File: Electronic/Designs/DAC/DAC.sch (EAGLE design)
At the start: 36 parts

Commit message: added new part to dac board
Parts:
- C5, C7: value 0.1uf -> 1uf
- JP1: value (none) -> PWR
- JP3: value (none) -> DIGITAL
- U$4: value OPA4227UA -> OPA2227UA; device OPAX22X:OPA4227UA -> OPAX22X:OPA2227UA
- renumbered JP4 to AOUT
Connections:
- net +15V: now also C4.1; no longer C5.1, U$2.V+
- net -15V: now also C5.1; no longer C4.1, U$2.V-
- net BIAS: now also U$4.OUTB; no longer U$4.OUTD
- net N$21: now also U$4.+INB; no longer U$4.+IND
- net N$22: now also U$4.-INB; no longer U$4.-IND
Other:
- moved on the sheet: JP1

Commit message: Added ADC board and schematic
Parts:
- JP2: value (none) -> AOUT
- renumbered AOUT to JP2
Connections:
- net +15V: now also U$2.V+
- net -15V: now also U$2.V-
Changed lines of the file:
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@@
 <part name="R22" library="resistor" deviceset="R-EU_" device="R0603" value="10k"/>
 <part name="SUPPLY9" library="supply2" deviceset="GND" device=""/>
-<part name="AOUT" library="pinhead" deviceset="PINHD-1X6" device=""/>
+<part name="JP2" library="pinhead" deviceset="PINHD-1X6" device="" value="AOUT"/>
 <part name="SUPPLY10" library="supply2" deviceset="GND" device=""/>
 <part name="JP3" library="pinhead" deviceset="PINHD-1X8" device="" value="DIGITAL"/>
@@
 <part name="SUPPLY28" library="supply2" deviceset="-15V" device=""/>
 <part name="SUPPLY29" library="supply2" deviceset="+15V" device=""/>
+<part name="SUPPLY30" library="supply2" deviceset="+15V" device=""/>
+<part name="SUPPLY31" library="supply2" deviceset="-15V" device=""/>
 </parts>
 <sheets>
@@
 <instance part="R22" gate="G$1" x="27.94" y="-48.26"/>
 <instance part="SUPPLY9" gate="GND" x="38.1" y="-50.8"/>
-<instance part="AOUT" gate="A" x="99.06" y="-99.06"/>
+<instance part="JP2" gate="A" x="99.06" y="-99.06"/>
 <instance part="SUPPLY10" gate="GND" x="88.9" y="-106.68"/>
 <instance part="JP3" gate="A" x="-50.8" y="0" rot="R180"/>
@@
 <instance part="SUPPLY28" gate="G$1" x="0" y="-38.1" rot="R180"/>
 <instance part="SUPPLY29" gate="+15V" x="5.08" y="-38.1"/>
+<instance part="SUPPLY30" gate="+15V" x="121.92" y="35.56"/>
+<instance part="SUPPLY31" gate="G$1" x="116.84" y="35.56" rot="R180"/>
 </instances>
 <busses>
@@
 <wire x1="0" y1="-40.64" x2="0" y2="-48.26" width="0.1524" layer="91"/>
 </segment>
+<segment>
+<pinref part="SUPPLY31" gate="G$1" pin="-15V"/>
+<pinref part="U$2" gate="G$1" pin="V-"/>
+<wire x1="116.84" y1="33.02" x2="116.84" y2="30.48" width="0.1524" layer="91"/>
+</segment>
 </net>
 <net name="+15V" class="0">
@@
 <wire x1="5.08" y1="-40.64" x2="5.08" y2="-48.26" width="0.1524" layer="91"/>
 </segment>
+<segment>
+<pinref part="SUPPLY30" gate="+15V" pin="+15V"/>
+<pinref part="U$2" gate="G$1" pin="V+"/>
+<wire x1="121.92" y1="33.02" x2="121.92" y2="30.48" width="0.1524" layer="91"/>
+</segment>
 </net>
 <net name="GND" class="0">
@@
 </segment>
 <segment>
-<pinref part="AOUT" gate="A" pin="6"/>
+<pinref part="JP2" gate="A" pin="6"/>
 <wire x1="96.52" y1="-104.14" x2="88.9" y2="-104.14" width="0.1524" layer="91"/>
 <pinref part="SUPPLY10" gate="GND" pin="GND"/>
@@
 </segment>
 <segment>
-<pinref part="AOUT" gate="A" pin="1"/>
+<pinref part="JP2" gate="A" pin="1"/>
 <wire x1="96.52" y1="-91.44" x2="88.9" y2="-91.44" width="0.1524" layer="91"/>
 <label x="83.82" y="-91.44" size="1.778" layer="95"/>
@@
 </segment>
 <segment>
-<pinref part="AOUT" gate="A" pin="2"/>
+<pinref part="JP2" gate="A" pin="2"/>
 <wire x1="96.52" y1="-93.98" x2="88.9" y2="-93.98" width="0.1524" layer="91"/>
 <label x="83.82" y="-93.98" size="1.778" layer="95"/>
@@
 </segment>
 <segment>
-<pinref part="AOUT" gate="A" pin="3"/>
+<pinref part="JP2" gate="A" pin="3"/>
 <wire x1="96.52" y1="-96.52" x2="88.9" y2="-96.52" width="0.1524" layer="91"/>
 <label x="83.82" y="-96.52" size="1.778" layer="95"/>
@@
 </segment>
 <segment>
-<pinref part="AOUT" gate="A" pin="4"/>
+<pinref part="JP2" gate="A" pin="4"/>
 <wire x1="96.52" y1="-99.06" x2="88.9" y2="-99.06" width="0.1524" layer="91"/>
 <label x="83.82" y="-99.06" size="1.778" layer="95"/>
@@
 </segment>
 <segment>
-<pinref part="AOUT" gate="A" pin="5"/>
+<pinref part="JP2" gate="A" pin="5"/>
 <wire x1="96.52" y1="-101.6" x2="88.9" y2="-101.6" width="0.1524" layer="91"/>
 <label x="83.82" y="-101.6" size="1.778" layer="95"/>
@@
 </sheet>
 </sheets>
+<errors>
+</errors>
 </schematic>
 </drawing>

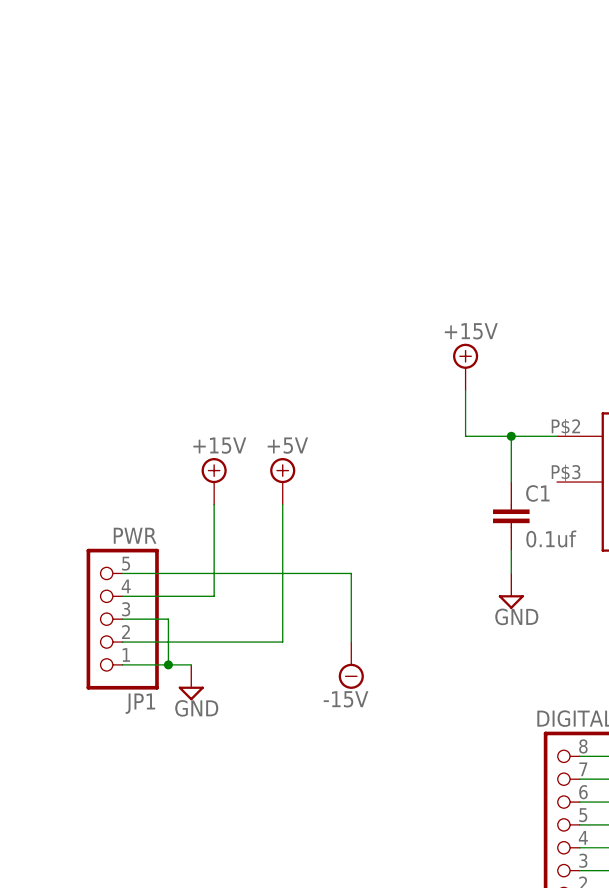
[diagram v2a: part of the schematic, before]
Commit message: split power pins from 5v and 15v
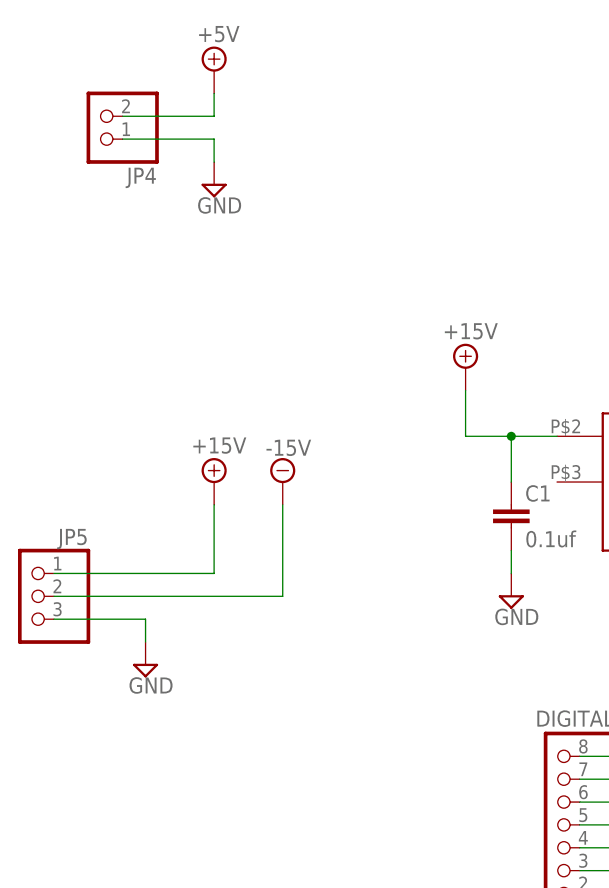
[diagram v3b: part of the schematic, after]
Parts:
- removed JP1: PWR, pinhead:PINHD-1X5
- added JP4: (no value), pinhead:PINHD-1X2
- added JP5: (no value), pinhead:PINHD-1X3
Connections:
- net +15V: now also JP5.1; no longer JP1.4
- net +5V: now also JP4.2; no longer JP1.2
- net -15V: now also JP5.2; no longer JP1.5
- net GND: now also JP4.1, JP5.3; no longer JP1.1, JP1.3
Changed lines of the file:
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@@
 <part name="U$2" library="OPAX22X" deviceset="OPA4227UA" device=""/>
 <part name="U$3" library="REF02" deviceset="REF02AU" device=""/>
-<part name="JP1" library="pinhead" deviceset="PINHD-1X5" device="" value="PWR"/>
 <part name="SUPPLY1" library="supply2" deviceset="GND" device=""/>
 <part name="SUPPLY2" library="supply2" deviceset="GND" device=""/>
@@
 <part name="SUPPLY30" library="supply2" deviceset="+15V" device=""/>
 <part name="SUPPLY31" library="supply2" deviceset="-15V" device=""/>
+<part name="JP4" library="pinhead" deviceset="PINHD-1X2" device=""/>
+<part name="JP5" library="pinhead" deviceset="PINHD-1X3" device=""/>
+<part name="SUPPLY32" library="supply2" deviceset="GND" device=""/>
 </parts>
 <sheets>
@@
 <instance part="U$2" gate="G$1" x="119.38" y="0"/>
 <instance part="U$3" gate="G$1" x="-35.56" y="43.18"/>
-<instance part="JP1" gate="A" x="-101.6" y="22.86" rot="R180"/>
-<instance part="SUPPLY1" gate="GND" x="-91.44" y="15.24"/>
+<instance part="SUPPLY1" gate="GND" x="-88.9" y="71.12"/>
 <instance part="SUPPLY2" gate="GND" x="-35.56" y="20.32"/>
 <instance part="SUPPLY3" gate="GND" x="0" y="-22.86"/>
@@
 <instance part="U$4" gate="G$1" x="2.54" y="-78.74"/>
 <instance part="SUPPLY18" gate="+15V" x="-88.9" y="38.1"/>
-<instance part="SUPPLY19" gate="G$1" x="-73.66" y="17.78"/>
+<instance part="SUPPLY19" gate="G$1" x="-81.28" y="38.1" rot="R180"/>
 <instance part="SUPPLY20" gate="+5V" x="-2.54" y="22.86"/>
 <instance part="SUPPLY21" gate="+5V" x="25.4" y="40.64"/>
-<instance part="SUPPLY22" gate="+5V" x="-81.28" y="38.1"/>
+<instance part="SUPPLY22" gate="+5V" x="-88.9" y="83.82"/>
 <instance part="SUPPLY23" gate="+15V" x="-60.96" y="50.8"/>
 <instance part="SUPPLY24" gate="+15V" x="134.62" y="60.96"/>
@@
 <instance part="SUPPLY30" gate="+15V" x="121.92" y="35.56"/>
 <instance part="SUPPLY31" gate="G$1" x="116.84" y="35.56" rot="R180"/>
+<instance part="JP4" gate="G$1" x="-101.6" y="78.74" rot="R180"/>
+<instance part="JP5" gate="A" x="-109.22" y="25.4" rot="MR0"/>
+<instance part="SUPPLY32" gate="GND" x="-96.52" y="17.78"/>
 </instances>
 <busses>
@@
 <nets>
 <net name="+5V" class="0">
-<segment>
-<pinref part="JP1" gate="A" pin="2"/>
-<pinref part="SUPPLY22" gate="+5V" pin="+5V"/>
-<wire x1="-99.06" y1="20.32" x2="-81.28" y2="20.32" width="0.1524" layer="91"/>
-<wire x1="-81.28" y1="20.32" x2="-81.28" y2="35.56" width="0.1524" layer="91"/>
-</segment>
 <segment>
 <pinref part="SUPPLY20" gate="+5V" pin="+5V"/>
@@
 <junction x="25.4" y="35.56"/>
 </segment>
+<segment>
+<pinref part="JP4" gate="G$1" pin="2"/>
+<pinref part="SUPPLY22" gate="+5V" pin="+5V"/>
+<wire x1="-99.06" y1="78.74" x2="-88.9" y2="78.74" width="0.1524" layer="91"/>
+<wire x1="-88.9" y1="78.74" x2="-88.9" y2="81.28" width="0.1524" layer="91"/>
+</segment>
 </net>
 <net name="-15V" class="0">
 <segment>
-<pinref part="JP1" gate="A" pin="5"/>
-<wire x1="-99.06" y1="27.94" x2="-73.66" y2="27.94" width="0.1524" layer="91"/>
-<wire x1="-73.66" y1="27.94" x2="-73.66" y2="20.32" width="0.1524" layer="91"/>
+<wire x1="-106.68" y1="25.4" x2="-81.28" y2="25.4" width="0.1524" layer="91"/>
+<wire x1="-81.28" y1="25.4" x2="-81.28" y2="35.56" width="0.1524" layer="91"/>
 <pinref part="SUPPLY19" gate="G$1" pin="-15V"/>
+<pinref part="JP5" gate="A" pin="2"/>
 </segment>
 <segment>
@@
 </segment>
 <segment>
-<pinref part="JP1" gate="A" pin="4"/>
 <pinref part="SUPPLY18" gate="+15V" pin="+15V"/>
-<wire x1="-99.06" y1="25.4" x2="-88.9" y2="25.4" width="0.1524" layer="91"/>
-<wire x1="-88.9" y1="25.4" x2="-88.9" y2="35.56" width="0.1524" layer="91"/>
+<wire x1="-88.9" y1="27.94" x2="-88.9" y2="35.56" width="0.1524" layer="91"/>
+<pinref part="JP5" gate="A" pin="1"/>
+<wire x1="-88.9" y1="27.94" x2="-106.68" y2="27.94" width="0.1524" layer="91"/>
 </segment>
 <segment>
@@
 </segment>
 <segment>
-<pinref part="JP1" gate="A" pin="1"/>
 <pinref part="SUPPLY1" gate="GND" pin="GND"/>
-<wire x1="-99.06" y1="17.78" x2="-93.98" y2="17.78" width="0.1524" layer="91"/>
-<pinref part="JP1" gate="A" pin="3"/>
-<wire x1="-93.98" y1="17.78" x2="-91.44" y2="17.78" width="0.1524" layer="91"/>
-<wire x1="-99.06" y1="22.86" x2="-93.98" y2="22.86" width="0.1524" layer="91"/>
-<wire x1="-93.98" y1="22.86" x2="-93.98" y2="17.78" width="0.1524" layer="91"/>
-<junction x="-93.98" y="17.78"/>
+<wire x1="-88.9" y1="73.66" x2="-88.9" y2="76.2" width="0.1524" layer="91"/>
+<pinref part="JP4" gate="G$1" pin="1"/>
+<wire x1="-88.9" y1="76.2" x2="-99.06" y2="76.2" width="0.1524" layer="91"/>
+</segment>
+<segment>
+<pinref part="JP5" gate="A" pin="3"/>
+<pinref part="SUPPLY32" gate="GND" pin="GND"/>
+<wire x1="-106.68" y1="22.86" x2="-96.52" y2="22.86" width="0.1524" layer="91"/>
+<wire x1="-96.52" y1="22.86" x2="-96.52" y2="20.32" width="0.1524" layer="91"/>
 </segment>
 </net>

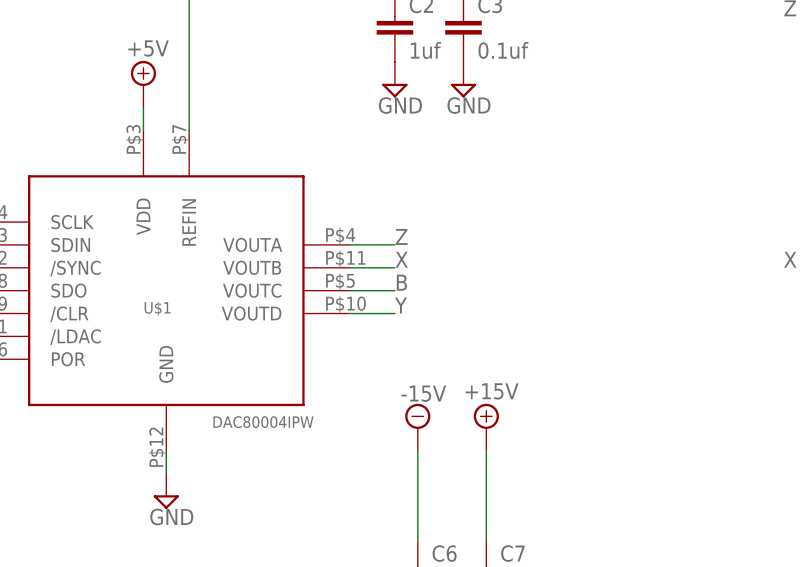
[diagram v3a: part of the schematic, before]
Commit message: added to dac pcb
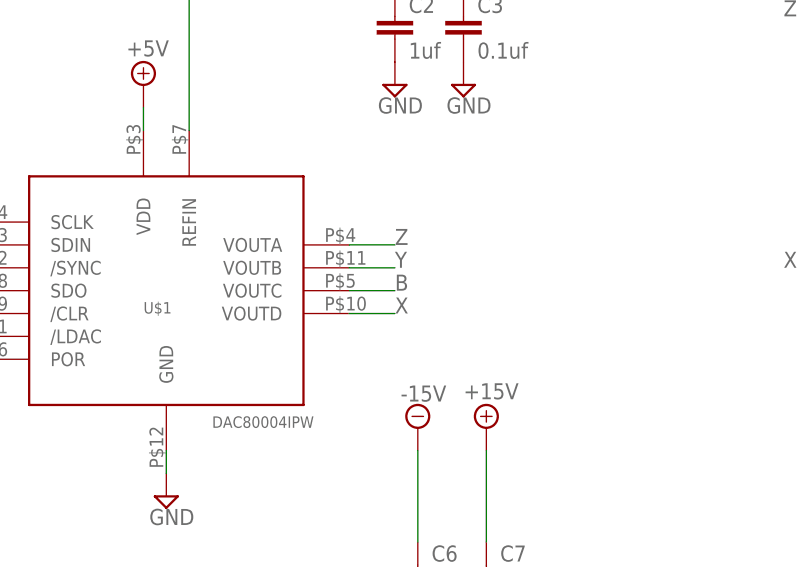
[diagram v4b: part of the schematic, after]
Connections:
- net X: now also U$1.VOUTD; no longer U$1.VOUTB
- net Y: now also U$1.VOUTB; no longer U$1.VOUTD
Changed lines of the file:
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@@
 </segment>
 <segment>
-<pinref part="U$1" gate="G$1" pin="VOUTB"/>
-<wire x1="20.32" y1="2.54" x2="25.4" y2="2.54" width="0.1524" layer="91"/>
-<label x="25.4" y="2.54" size="1.778" layer="95"/>
+<pinref part="U$1" gate="G$1" pin="VOUTD"/>
+<wire x1="20.32" y1="-2.54" x2="25.4" y2="-2.54" width="0.1524" layer="91"/>
+<label x="25.4" y="-2.54" size="1.778" layer="95"/>
 </segment>
 </net>
@@
 </segment>
 <segment>
-<pinref part="U$1" gate="G$1" pin="VOUTD"/>
-<wire x1="20.32" y1="-2.54" x2="25.4" y2="-2.54" width="0.1524" layer="91"/>
-<label x="25.4" y="-2.54" size="1.778" layer="95"/>
+<pinref part="U$1" gate="G$1" pin="VOUTB"/>
+<wire x1="20.32" y1="2.54" x2="25.4" y2="2.54" width="0.1524" layer="91"/>
+<label x="25.4" y="2.54" size="1.778" layer="95"/>
 </segment>
 </net>
